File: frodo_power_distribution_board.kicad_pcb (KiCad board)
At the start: 2 copper layers, 27 parts, among them J1 Payload_1, J2 Payload_2, J3 Payload_3, J4 Conn_01x06, J5 Conn_01x06

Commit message: First iteration of board layout
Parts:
- moved C4 49.5 mm to (92.6, 96.5)
- moved C1 48.0 mm to (92.6, 92.7)
- moved C7 43.9 mm to (92.6, 101.5)
- moved D1 39.7 mm to (92.8, 87.2)
- moved D4 34.9 mm to (103.0, 102.3), turned to -90 degrees
- moved F1 34.1 mm to (103.0, 93.0), turned to -90 degrees
- moved C5 31.8 mm to (110.4, 97.3)
- moved C2 29.6 mm to (110.7, 92.5)
- moved C8 26.6 mm to (110.5, 102.1)
- moved D2 24.3 mm to (110.7, 87.4)
- moved D5 20.0 mm to (118.2, 102.3), turned to -90 degrees
- moved F2 19.9 mm to (118.2, 93.0), turned to -90 degrees
- moved D3 17.3 mm to (125.3, 87.4)
- moved C6 16.9 mm to (126.0, 97.3)
- moved C3 14.1 mm to (125.8, 92.3)
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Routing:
- net VDC: track 0.00 -> 59.8 mm
- net Net-(D2-K): track 0.00 -> 31.2 mm
- net Net-(D3-K): track 0.00 -> 30.9 mm
- net Net-(D1-K): track 0.00 -> 30.7 mm
- net CAN-: track 0.00 -> 19.6 mm
- net CAN+: track 0.00 -> 19.1 mm
- net Net-(J4-Pin_5): track 0.00 -> 19.0 mm
- net Net-(D6-K): track 0.00 -> 6.22 mm
- net Net-(D5-K): track 0.00 -> 5.96 mm
- net Net-(D4-K): track 0.00 -> 5.96 mm
- added copper zone on B.Cu, net GND
- added copper zone on F.Cu, net GND
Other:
- board outline added: 58 x 58 mm

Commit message: Add missing connection
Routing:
- net Net-(D3-K): track 30.9 -> 49.2 mm
- net Net-(D2-K): track 31.2 -> 47.8 mm
- net Net-(D1-K): track 30.7 -> 46.4 mm
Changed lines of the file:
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@@
+	)
+	(segment
+		(start 102.997 91.567)
+		(end 102.997 79.0708)
+		(width 0.2)
+		(layer "F.Cu")
+		(net 1)
 	)
 	(segment
@@
 	)
 	(segment
+		(start 102.997 79.0708)
+		(end 100.7124 76.7862)
+		(width 0.2)
+		(layer "F.Cu")
+		(net 1)
+	)
+	(segment
 		(start 97.7124 76.7862)
 		(end 100.7124 76.7862)
@@
 	)
 	(segment
+		(start 118.237 81.2806)
+		(end 113.7426 76.7862)
+		(width 0.2)
+		(layer "F.Cu")
+		(net 3)
+	)
+	(segment
 		(start 109.347 101.854)
 		(end 109.601 102.108)
@@
 	)
 	(segment
+		(start 118.237 91.567)
+		(end 118.237 81.2806)
+		(width 0.2)
+		(layer "F.Cu")
+		(net 3)
+	)
+	(segment
 		(start 109.093 92.456)
 		(end 109.093 97.028)
@@
 	)
 	(segment
+		(start 134.877 91.437)
+		(end 134.877 85.6016)
+		(width 0.2)
+		(layer "F.Cu")
+		(net 4)
+	)
+	(segment
 		(start 123.7488 87.376)
 		(end 123.949 87.376)
@@
 		(width 0.2)
 		(layer "F.Cu")
+		(net 4)
+	)
+	(segment
+		(start 134.877 85.6016)
+		(end 126.0362 76.7608)
+		(width 0.2)
+		(layer "F.Cu")

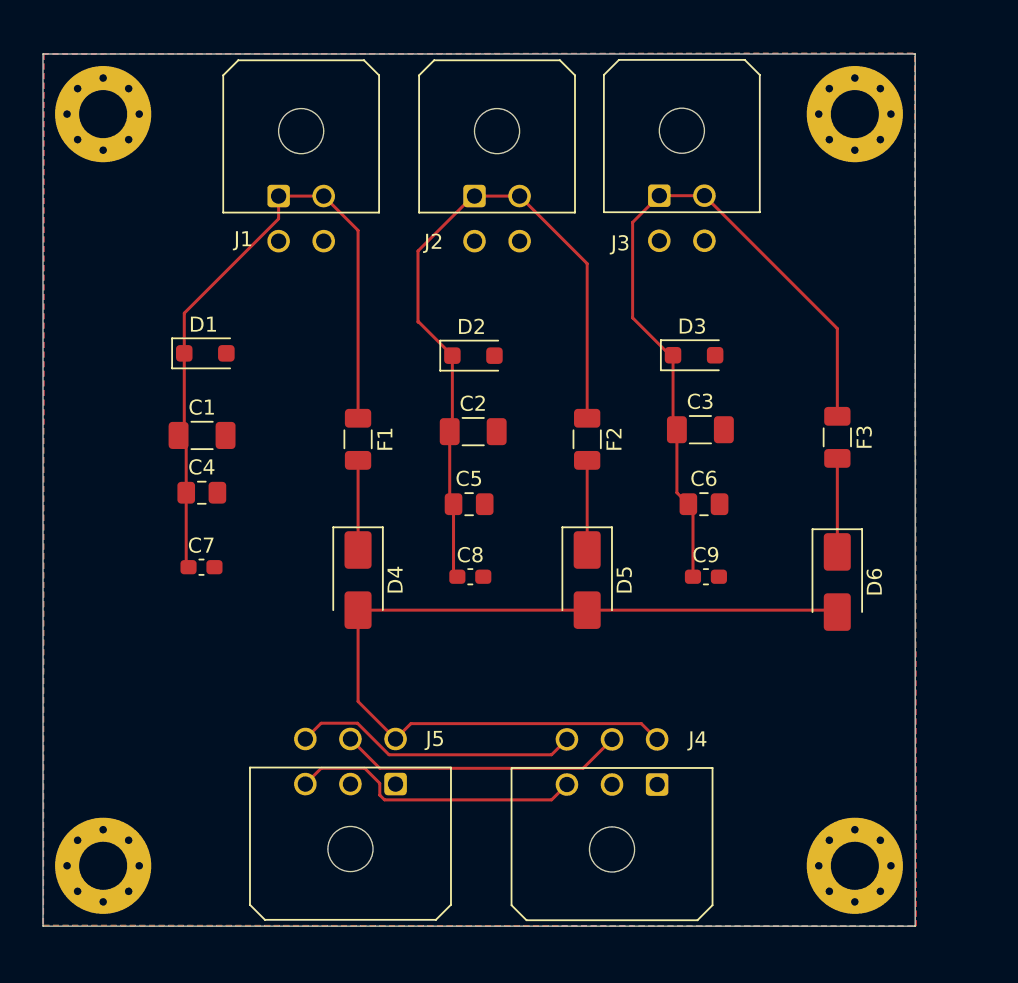
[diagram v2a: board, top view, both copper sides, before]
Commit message: Round off edges, skew CAN, widen traces
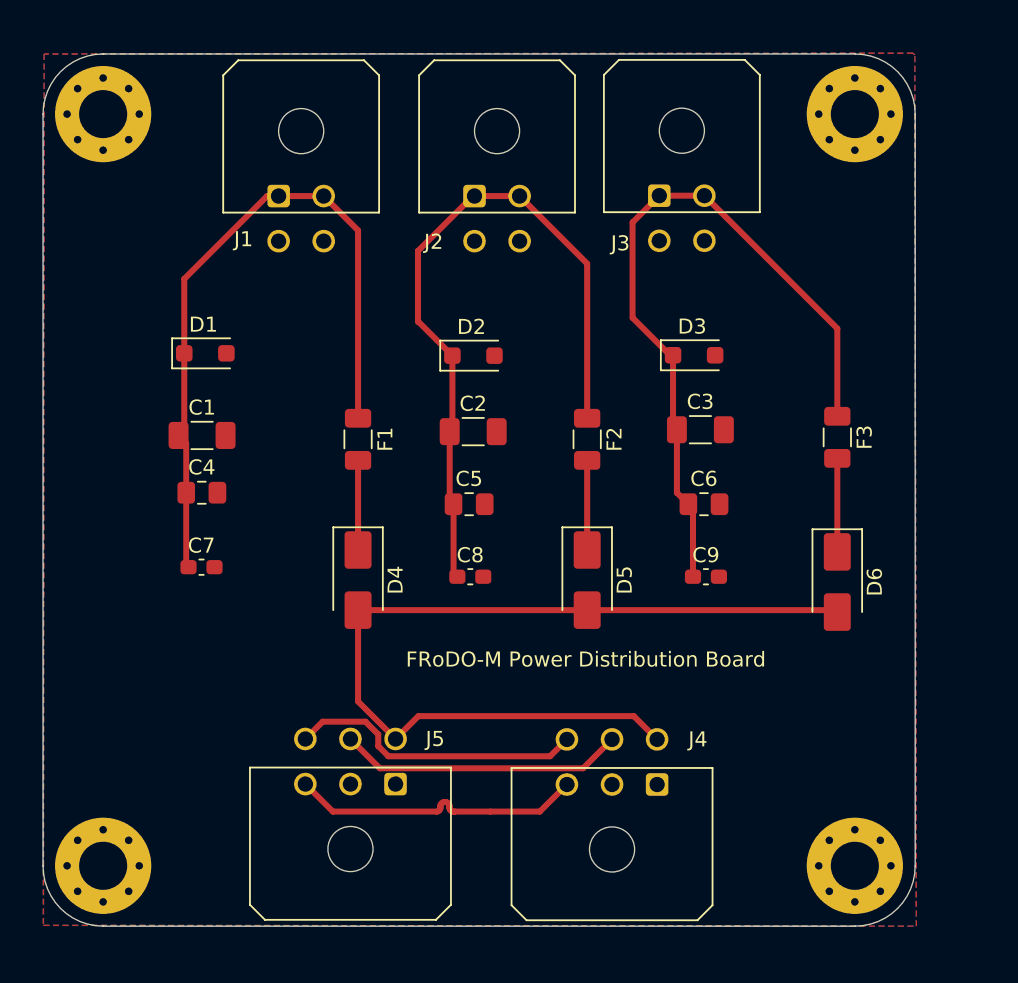
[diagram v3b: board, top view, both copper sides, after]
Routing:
- net CAN+: track 19.1 -> 19.7 mm
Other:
- outline, holes or cut-outs redrawn
- board text added: "FRoDO-M Power Distribution Board"

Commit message: Fatten traces, remove thermal relief, fix 2x2 pinout, move filter components inline
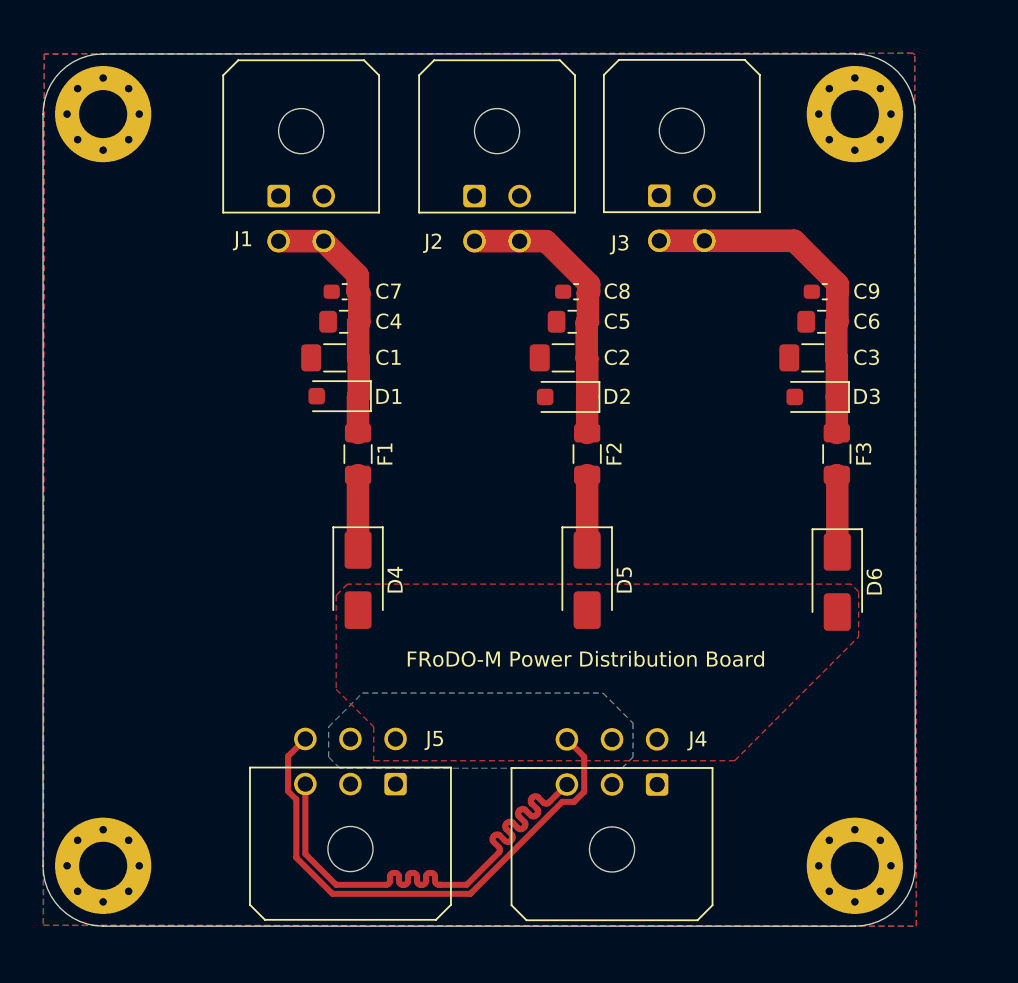
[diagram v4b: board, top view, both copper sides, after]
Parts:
- moved C7 20.7 mm to (102.1, 83.1), turned to 180 degrees
- moved C9 20.5 mm to (134.0, 83.1), turned to 180 degrees
- moved C8 20.2 mm to (117.5, 83.1), turned to 180 degrees
- moved C4 14.8 mm to (102.0, 85.1), turned to 180 degrees
- moved C6 14.4 mm to (133.8, 85.1), turned to 180 degrees
- moved C5 13.9 mm to (117.2, 85.1), turned to 180 degrees
- moved C1 10.2 mm to (101.4, 87.5), turned to 180 degrees
- moved D1 9.25 mm to (101.6, 90.1), turned to 180 degrees
- moved C3 8.87 mm to (133.2, 87.5), turned to 180 degrees
- moved D3 8.55 mm to (133.4, 90.1), turned to 180 degrees
- moved C2 7.74 mm to (116.6, 87.5), turned to 180 degrees
- moved D2 6.76 mm to (116.8, 90.1), turned to 180 degrees
- moved F3 1.11 mm to (134.8, 93.9)
- moved F1 0.98 mm to (103.0, 93.9)
- moved F2 0.98 mm to (118.2, 93.9)
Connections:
- J1 pad 1: Net-(D1-K) -> GND
- J1 pad 2: Net-(D1-K) -> GND
- J1 pad 3: GND -> Net-(D1-K)
- J1 pad 4: GND -> Net-(D1-K)
- J2 pad 1: Net-(D2-K) -> GND
- J2 pad 2: Net-(D2-K) -> GND
- J2 pad 3: GND -> Net-(D2-K)
- J2 pad 4: GND -> Net-(D2-K)
- J3 pad 1: Net-(D3-K) -> GND
- J3 pad 2: Net-(D3-K) -> GND
- J3 pad 3: GND -> Net-(D3-K)
- J3 pad 4: GND -> Net-(D3-K)
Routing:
- net VDC: track 60.2 -> 0.00 mm
- net Net-(D1-K): track 46.9 -> 16.8 mm
- net Net-(D2-K): track 47.8 -> 18.8 mm
- net Net-(D3-K): track 49.2 -> 23.0 mm
- net Net-(J4-Pin_5): track 19.0 -> 0.00 mm
- net CAN+: track 19.7 -> 35.5 mm
- net CAN-: track 19.7 -> 35.2 mm
- net Net-(D6-K): track 6.22 -> 5.12 mm
- net Net-(D5-K): track 5.96 -> 4.98 mm
- net Net-(D4-K): track 5.96 -> 4.98 mm
- added copper zone on B.Cu, net Net-(J4-Pin_5)
- added copper zone on F.Cu, net VDC

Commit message: Make pretty
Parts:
- added G***: LOGO, frodo_power_distribution_board:rapid_logo, F.Cu at (92.3, 103.2)
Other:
- board text added: "JLCJLCJLCJLC"
- board text added: "rev 1"
